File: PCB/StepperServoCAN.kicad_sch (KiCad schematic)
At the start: 132 parts, among them J1 CAR, J2 Debug, J3 Motor, J4 Conn_01x06, Q1 AO3401A, Q2 2N7002, Q3 AO3401A, SW1 Rst, SW2 Fcn>, SW3 Fcn>, U2 STM32F103CBT6, U3 LMV321, U4 AT8236, U5 DRV8870, U6 LMV321, U7 TLE5012B, U8 TMAG5170-Q1, U9 SN65HVD230, Y1 16Mhz 9pF

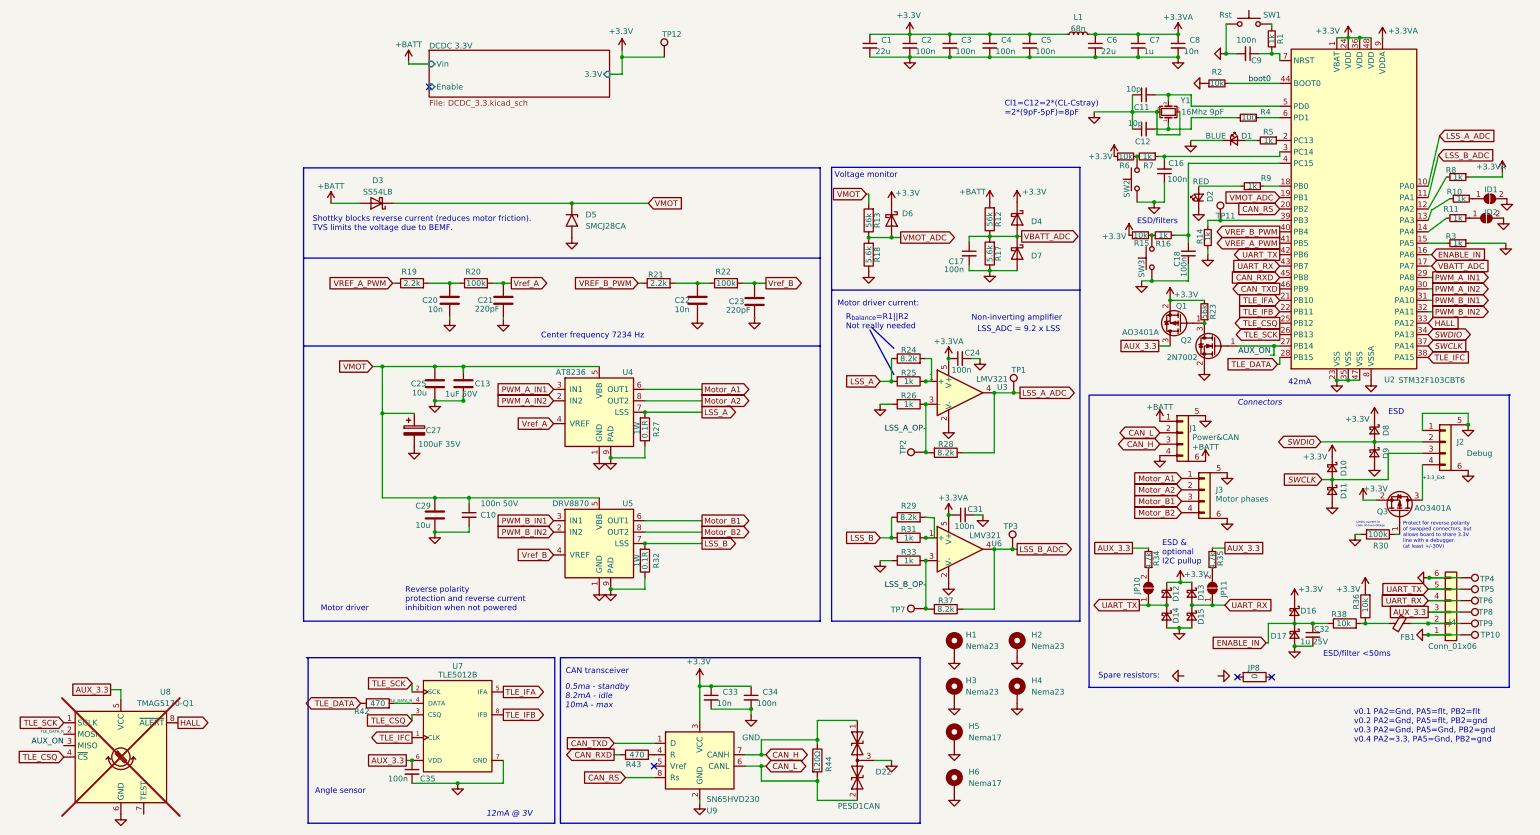
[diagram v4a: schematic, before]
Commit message: ability to fully shutdown on low voltage. Power back on above 11V.
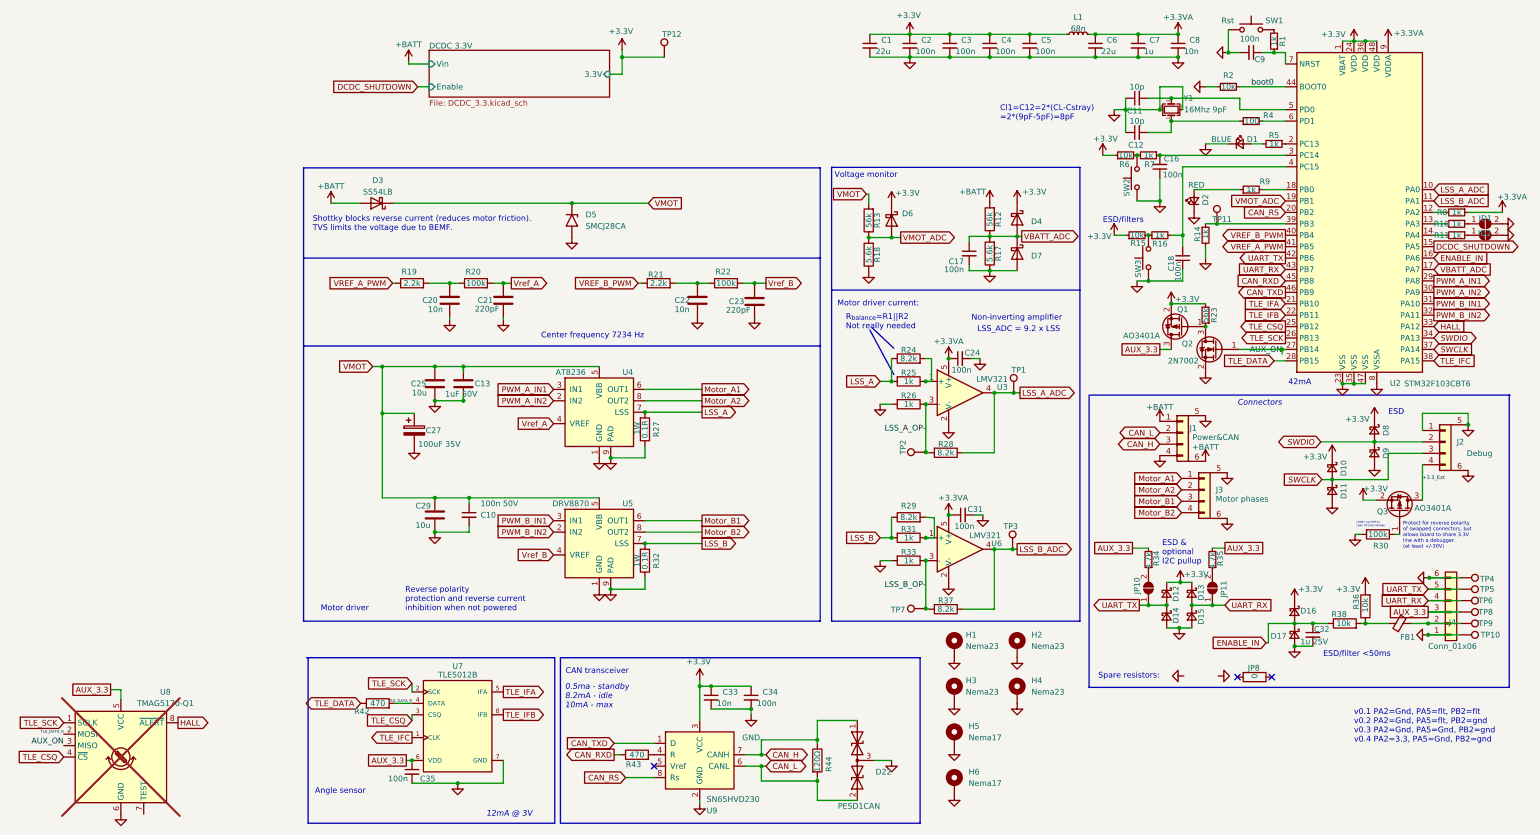
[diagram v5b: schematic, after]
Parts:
- removed R3: 1k, Resistor_SMD:R_0402_1005Metric, symbol Device:R_Small
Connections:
- net DCDC_SHUTDOWN: now reaches U2.15 (PA5)
- no-connect marks 4 -> 3
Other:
- moved on the sheet: C11, C12, C16, C18, C9, D1, D2, ID1, ID2, Q1, Q2, R1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

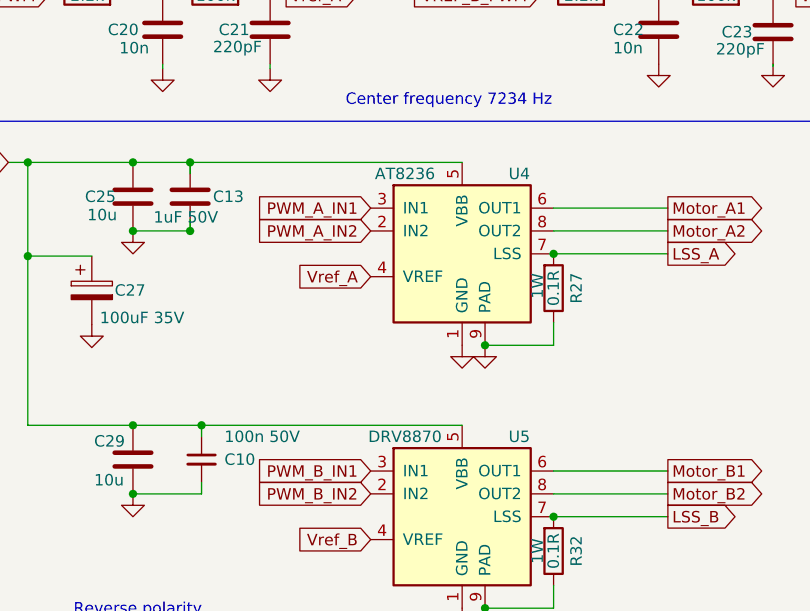
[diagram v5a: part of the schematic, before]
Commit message: Reverted AT8236 back to A4950 for better current control capabilities
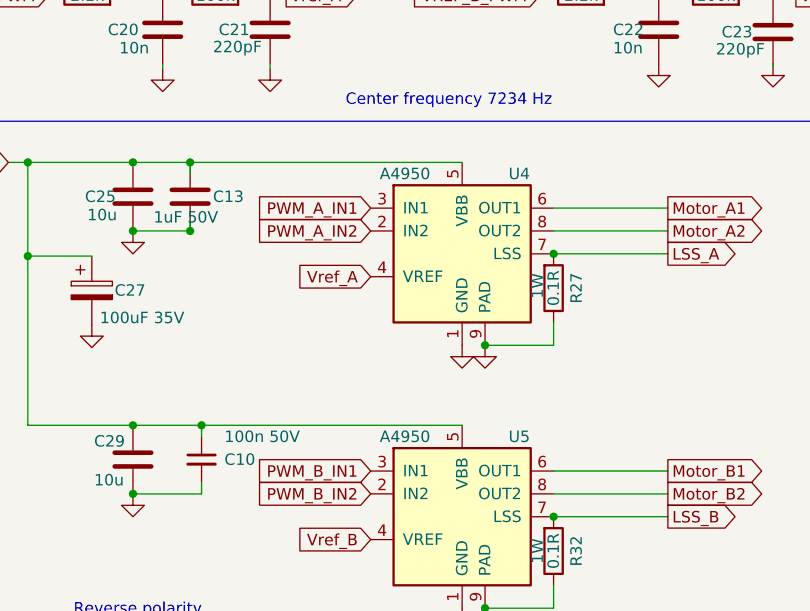
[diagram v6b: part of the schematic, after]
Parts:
- U4: value AT8236 -> A4950; LCSC C2827823 -> C82404
- U5: value DRV8870 -> A4950; LCSC C86590 -> C82404
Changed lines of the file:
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@@
 			)
 		)
-		(property "Value" "AT8236"
+		(property "Value" "A4950"
 			(at 74.676 93.98 0)
 			(effects
@@
 			)
 		)
-		(property "Datasheet" "https://wmsc.lcsc.com/wmsc/upload/file/pdf/v2/lcsc/2109242230_ZHONGKEWEI-AT8236_C2827823.pdf"
+		(property "Datasheet" "https://www.allegromicro.com/-/media/files/datasheets/a4950-datasheet.ashx"
 			(at 73.406 93.98 0)
 			(effects
@@
 			)
 		)
-		(property "LCSC" "C2827823"
+		(property "LCSC" "C82404"
 			(at 87.376 93.98 0)
 			(effects
@@
 			)
 		)
-		(property "Value" "DRV8870"
+		(property "Value" "A4950"
 			(at 74.676 123.19 0)
 			(effects
@@
 			)
 		)
-		(property "Datasheet" "https://www.ti.com/lit/ds/symlink/drv8870.pdf"
+		(property "Datasheet" "https://www.allegromicro.com/-/media/files/datasheets/a4950-datasheet.ashx"
 			(at 73.406 123.19 0)
 			(effects
@@
 			)
 		)
-		(property "LCSC" "C86590"
+		(property "LCSC" "C82404"
 			(at 87.376 123.19 0)
 			(effects

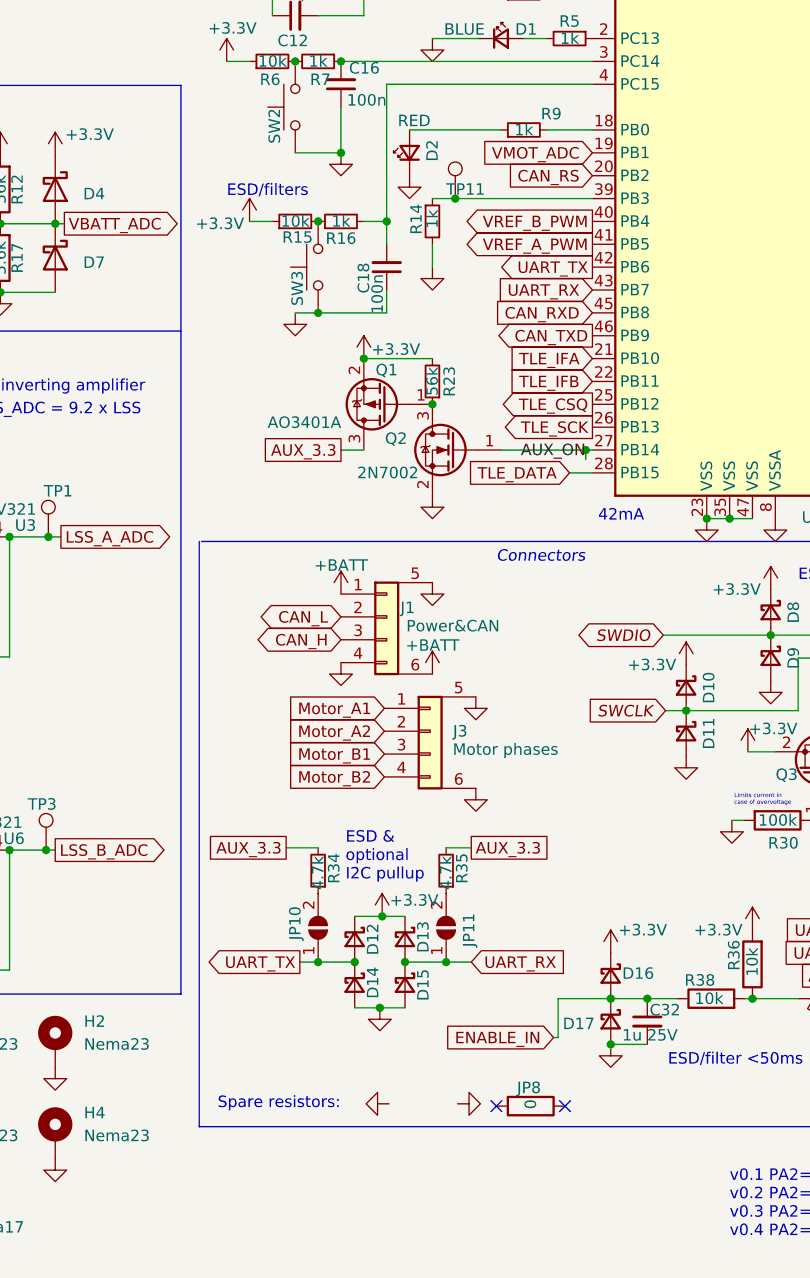
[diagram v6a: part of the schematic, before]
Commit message: Moved some signals to inner layer to free up top ground for better thermals
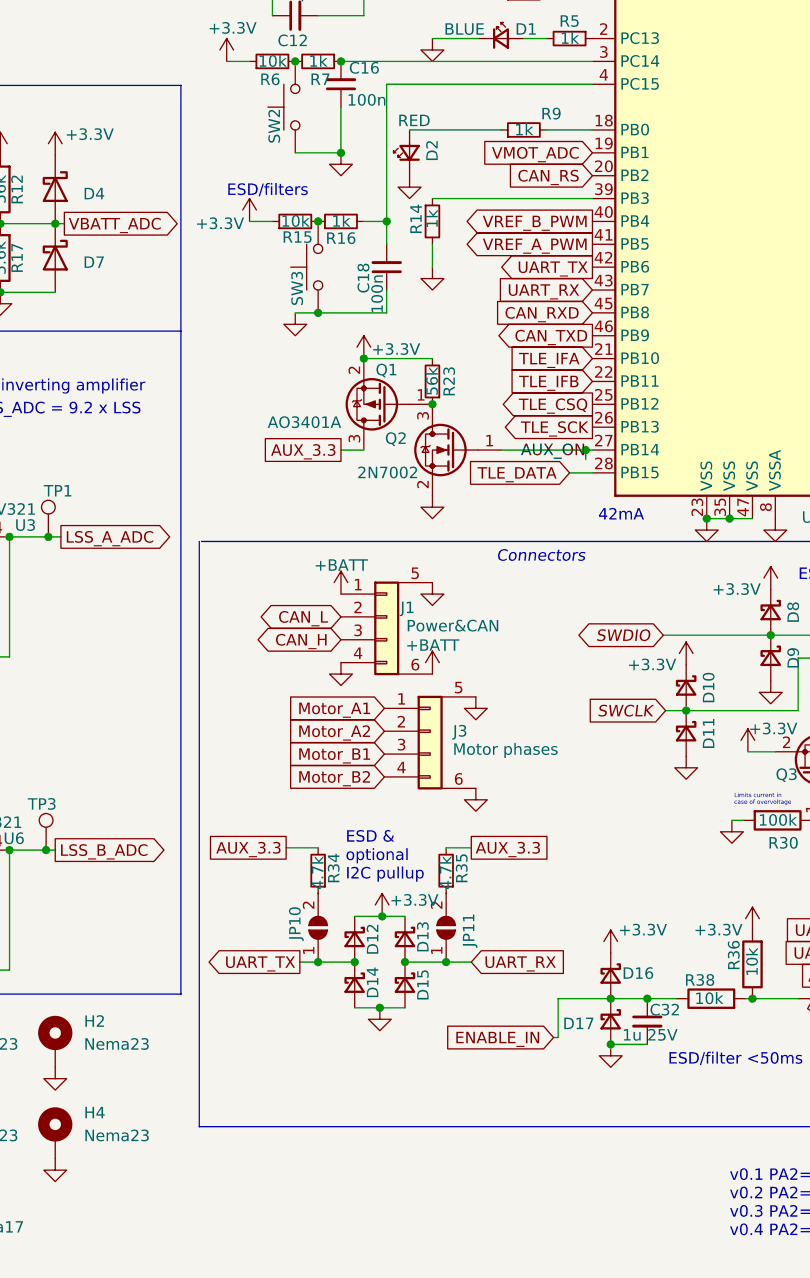
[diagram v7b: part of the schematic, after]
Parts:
- removed JP8: 0, Resistor_SMD:R_0805_2012Metric, symbol Device:R
- removed TP11: Pad, TestPoint:TestPoint_Pad_D1.0mm, symbol Connector:TestPoint
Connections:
- no-connect marks 3 -> 1
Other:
- note removed: "Spare resistors:"

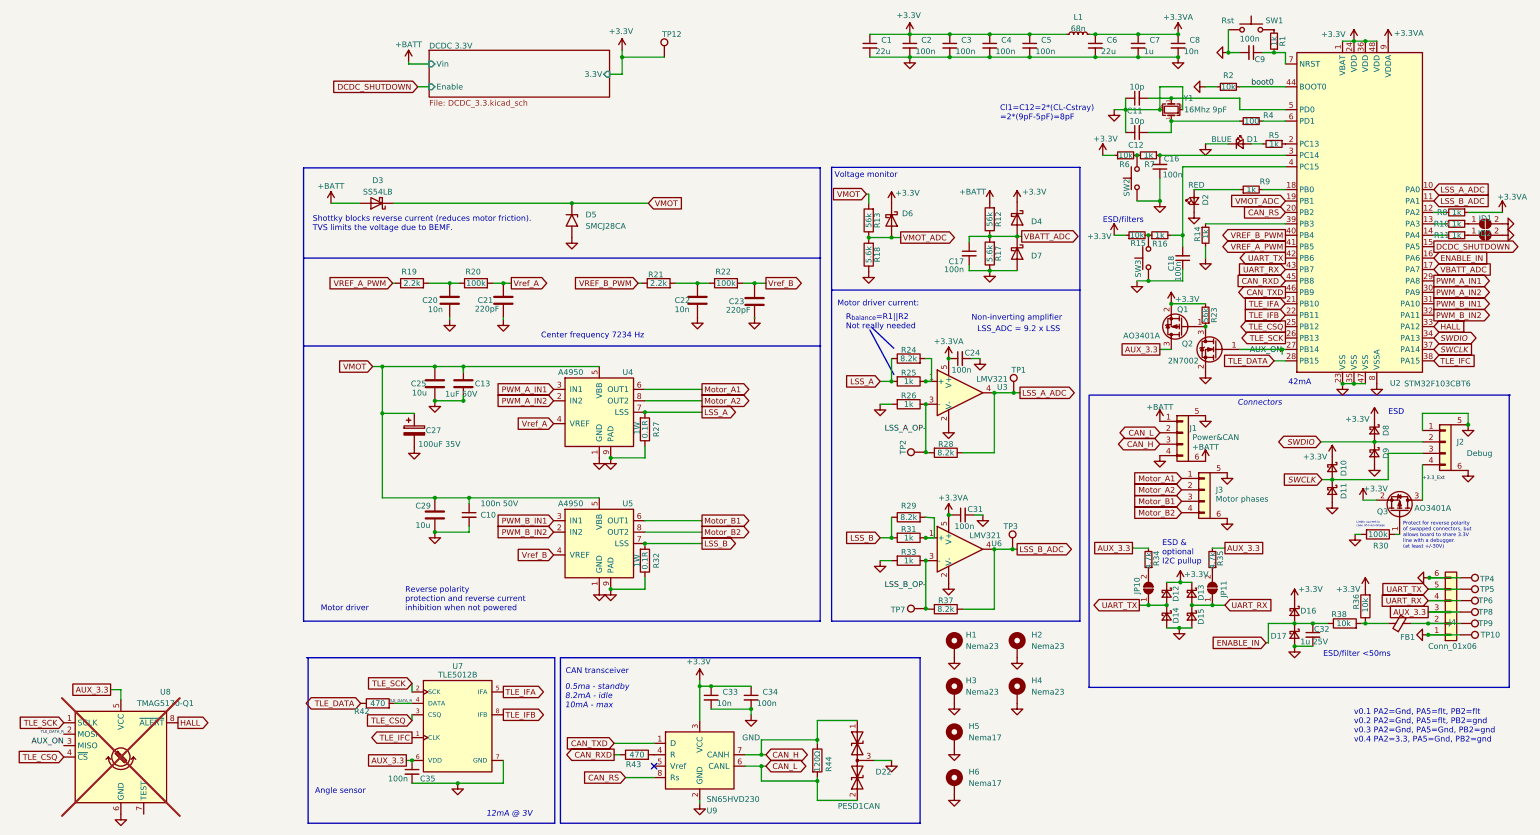
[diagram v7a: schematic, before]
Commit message: Moved experimental TLE_IF (encoder) interface to dedicated channel 2 of tim2
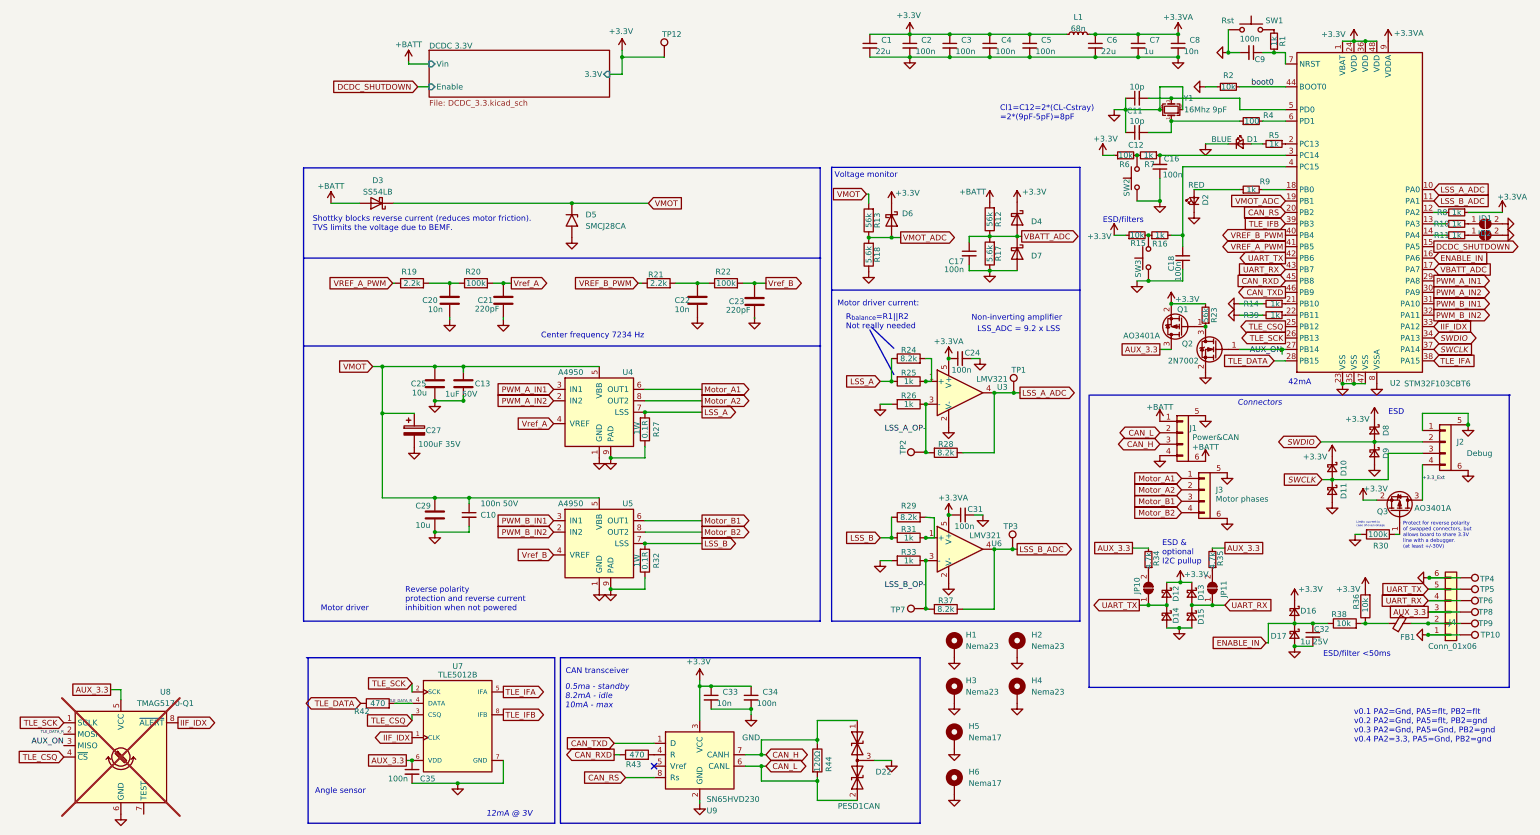
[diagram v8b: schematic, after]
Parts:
- added R39: 1k, Resistor_SMD:R_0402_1005Metric, symbol Device:R_Small
- D5: Note (none) -> Unidirectional could be slightly stronger, but bi was cheap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
- U7: Component Link 1 Description Manufacturer URL -> (none); Component Link 1 URL http://www.infineon.com/ -> (none); Component Link 3 Description Package Specification -> (none); Component Link 3 URL http://www.infineon.com/dgdl/TLE7259-2GE_DS_rev12.pdf?folde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 -> (none); Datasheet Version Rev. 1.0 -> (none); Green true -> (none); Halogen free available -> (none); Package Version Mar-07 -> (none); Packing Reel -> (none); category IC -> (none); ciiva ids 2417005 -> (none); imported yes -> (none); library id 1b15dfdf5dbbaf04 -> (none); release date 1409234811 -> (none); vault revision E581E8E0-9BC8-4E10-9C4E-2BCCB84CD538 -> (none)
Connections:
- net GND: now also R39.2
- net TLE_IFA: now also U2.38 (PA15); no longer U2.21 (PB10)
- net TLE_IFB: now also U2.39 (PB3); no longer U2.22 (PB11)
- net at R14.1: now also U2.21 (PB10); no longer U2.39 (PB3)
- net HALL renamed IIF_IDX
- net IIF_IDX: now also U7.1 (CLK)
- removed net TLE_IFC: U2.38 (PA15), U7.1 (CLK)
- new net: R39.1, U2.22 (PB11)
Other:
- moved on the sheet: R14
